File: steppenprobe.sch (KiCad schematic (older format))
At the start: 84 parts, among them J1 USB_C_Receptacle_USB2.0, J2 Conn_ST_STDC14, J4 Conn_01x16, Q1 2N7002, SW1 SW_SPDT, SW2 SW_Push, U1 FT2232H, U10 74LVC1G125, U11 74LVC1G125, U12 74LVC1G125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

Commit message: Replace FT2232H by FT2232HL
Old symbol is no longer in the library. It was a common symbol for
both LQFP and QFN and it is now individual symbols for different
packages.
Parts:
- U1: value FT2232H -> FT2232HL; symbol Interface_USB:FT2232H -> Interface_USB:FT2232HL
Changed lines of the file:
@@
 GPIO_A
 $Comp
-L Interface_USB:FT2232H U1
+L Interface_USB:FT2232HL U1
 U 1 1 5C60DA40
 P 7200 5950
 F 0 "U1" H 6200 8050 50  0000 C CNN
-F 1 "FT2232H" H 8100 8050 50  0000 C CNN
+F 1 "FT2232HL" H 8100 8050 50  0000 C CNN
 F 2 "Package_QFP:LQFP-64_10x10mm_P0.5mm" H 7200 5950 50  0001 C CNN
-F 3 "http://www.ftdichip.com/Products/ICs/FT2232H.html" H 7200 5950 50  0001 C CNN
+F 3 "https://www.ftdichip.com/Support/Documents/DataSheets/ICs/DS_FT2232H.pdf" H 7200 5950 50  0001 C CNN
 F 4 "FTDI" H 7200 5950 50  0001 C CNN "Manufacturer"
 F 5 "FT2232HL" H 7200 5950 50  0001 C CNN "MPN"

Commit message: Move 74xxGxx to a project library
The symbols in the upstream libraries use hidden power pins which
doesn't work in this design which needs different power rails on
different instances.

So far, a private modifed branch of the libraries was used. But,
becasue the upstream library won't be fix until KiCad 6 for
compatibility reasons, a project library has been created which
makes it easier to share this project.
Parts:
- U10, U11, U12, U5, U7, U8, U9: symbol 74xGxx:74LVC1G125 -> 74xxGxx_power_pins:74LVC1G125-74xGxx
- U6: symbol 74xGxx:74LVC1G126 -> 74xxGxx_power_pins:74LVC1G126-74xGxx
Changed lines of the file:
@@
 	11700 2800 11700 2750
 $Comp
-L 74xGxx:74LVC1G125 U8
+L 74xxGxx_power_pins:74LVC1G125-74xGxx U8
 U 1 1 5CA2CD85
 P 11800 2550
@@
 $EndComp
 $Comp
-L 74xGxx:74LVC1G125 U7
+L 74xxGxx_power_pins:74LVC1G125-74xGxx U7
 U 1 1 5C73B9C7
 P 11800 1650
@@
 	11750 3250 11750 3200
 $Comp
-L 74xGxx:74LVC1G125 U5
+L 74xxGxx_power_pins:74LVC1G125-74xGxx U5
 U 1 1 5C93EC63
 P 11750 3450
@@
 $EndComp
 $Comp
-L 74xGxx:74LVC1G125 U9
+L 74xxGxx_power_pins:74LVC1G125-74xGxx U9
 U 1 1 5C955E12
 P 11800 5200
@@
 $EndComp
 $Comp
-L 74xGxx:74LVC1G125 U10
+L 74xxGxx_power_pins:74LVC1G125-74xGxx U10
 U 1 1 5C980186
 P 11850 6350
@@
 	10850 3200 10850 4150
 $Comp
-L 74xGxx:74LVC1G126 U6
+L 74xxGxx_power_pins:74LVC1G126-74xGxx U6
 U 1 1 5CB0C088
 P 11750 4400
@@
 $EndComp
 $Comp
-L 74xGxx:74LVC1G125 U11
+L 74xxGxx_power_pins:74LVC1G125-74xGxx U11
 U 1 1 5C926BFE
 P 11850 8550
@@
 $EndComp
 $Comp
-L 74xGxx:74LVC1G125 U12
+L 74xxGxx_power_pins:74LVC1G125-74xGxx U12
 U 1 1 5C8DEFEB
 P 11900 7400

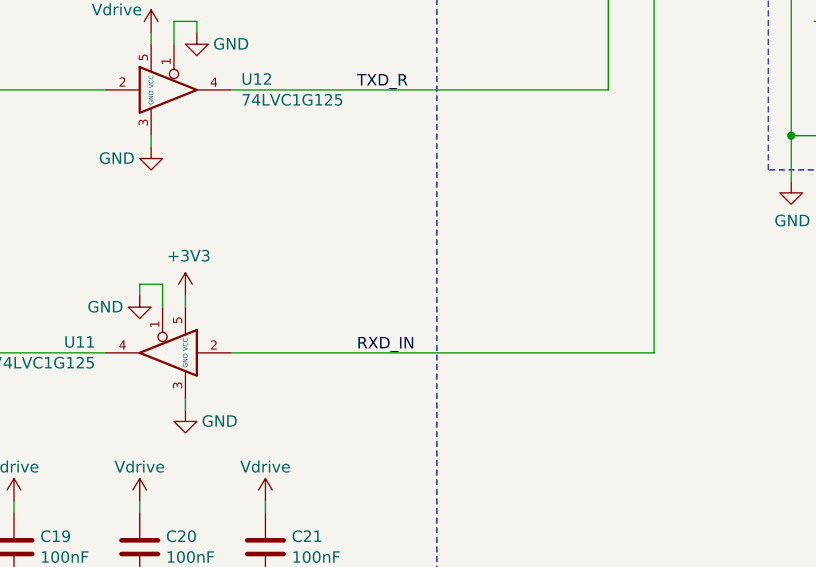
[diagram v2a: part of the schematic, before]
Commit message: Add pull up resistor to RXD_IN
To avoid spurious RX when floating.

Also some small tidy up of silkscreen designators.
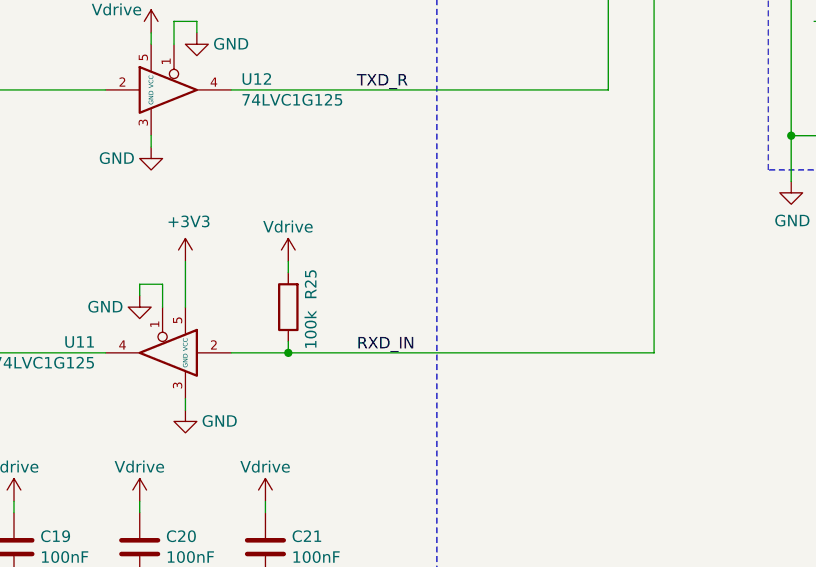
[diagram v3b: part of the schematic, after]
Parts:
- added R25: 100k, Resistor_SMD:R_0603_1608Metric, symbol Device:R
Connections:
- wire segments 370 -> 373
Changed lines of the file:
@@
 	12150 7400 13800 7400
-$Comp
-L power:+3V3 #PWR049
-U 1 1 5C93BEDD
-P 11950 8300
-F 0 "#PWR049" H 11950 8150 50  0001 C CNN
-F 1 "+3V3" H 11965 8473 50  0000 C CNN
-F 2 "" H 11950 8300 50  0001 C CNN
-F 3 "" H 11950 8300 50  0001 C CNN
-	1    11950 8300
-	1    0    0    -1
-$EndComp
 $Comp
 L 74xxGxx_power_pins:74LVC1G125-74xGxx U11
@@
 $EndComp
 Wire Wire Line
-	11950 8350 11950 8300
-Wire Wire Line
-	12150 8550 14000 8550
-Wire Wire Line
 	11600 8550 10750 8550
 Wire Wire Line
@@
 Text Label 8450 5550 0    50   ~ 0
 GPIO_D
+$Comp
+L Device:R R25
+U 1 1 5E57A95D
+P 12400 8350
+F 0 "R25" V 12300 8250 50  0000 C CNN
+F 1 "100k" V 12300 8450 50  0000 C CNN
+F 2 "Resistor_SMD:R_0603_1608Metric" V 12330 8350 50  0001 C CNN
+F 3 "~" H 12400 8350 50  0001 C CNN
+F 4 "C25803" H 12400 8350 50  0001 C CNN "LCSC_PN"
+	1    12400 8350
+	-1   0    0    1
+$EndComp
+Wire Wire Line
+	11950 8350 11950 8150
+$Comp
+L power:+3V3 #PWR049
+U 1 1 5C93BEDD
+P 11950 8150
+F 0 "#PWR049" H 11950 8000 50  0001 C CNN
+F 1 "+3V3" H 11965 8323 50  0000 C CNN
+F 2 "" H 11950 8150 50  0001 C CNN
+F 3 "" H 11950 8150 50  0001 C CNN
+	1    11950 8150
+	1    0    0    -1
+$EndComp
+Wire Wire Line
+	12400 8550 14000 8550
+Connection ~ 12400 8550
+Wire Wire Line
+	12150 8550 12400 8550
+Wire Wire Line
+	12400 8550 12400 8500
+Wire Wire Line
+	12400 8150 12400 8200
+$Comp
+L power:Vdrive #PWR067
+U 1 1 5E57CDC9
+P 12400 8150
+F 0 "#PWR067" H 12200 8000 50  0001 C CNN
+F 1 "Vdrive" H 12400 8300 50  0000 C CNN
+F 2 "" H 12400 8150 50  0001 C CNN
+F 3 "" H 12400 8150 50  0001 C CNN
+	1    12400 8150
+	1    0    0    -1
+$EndComp
 $EndSCHEMATC

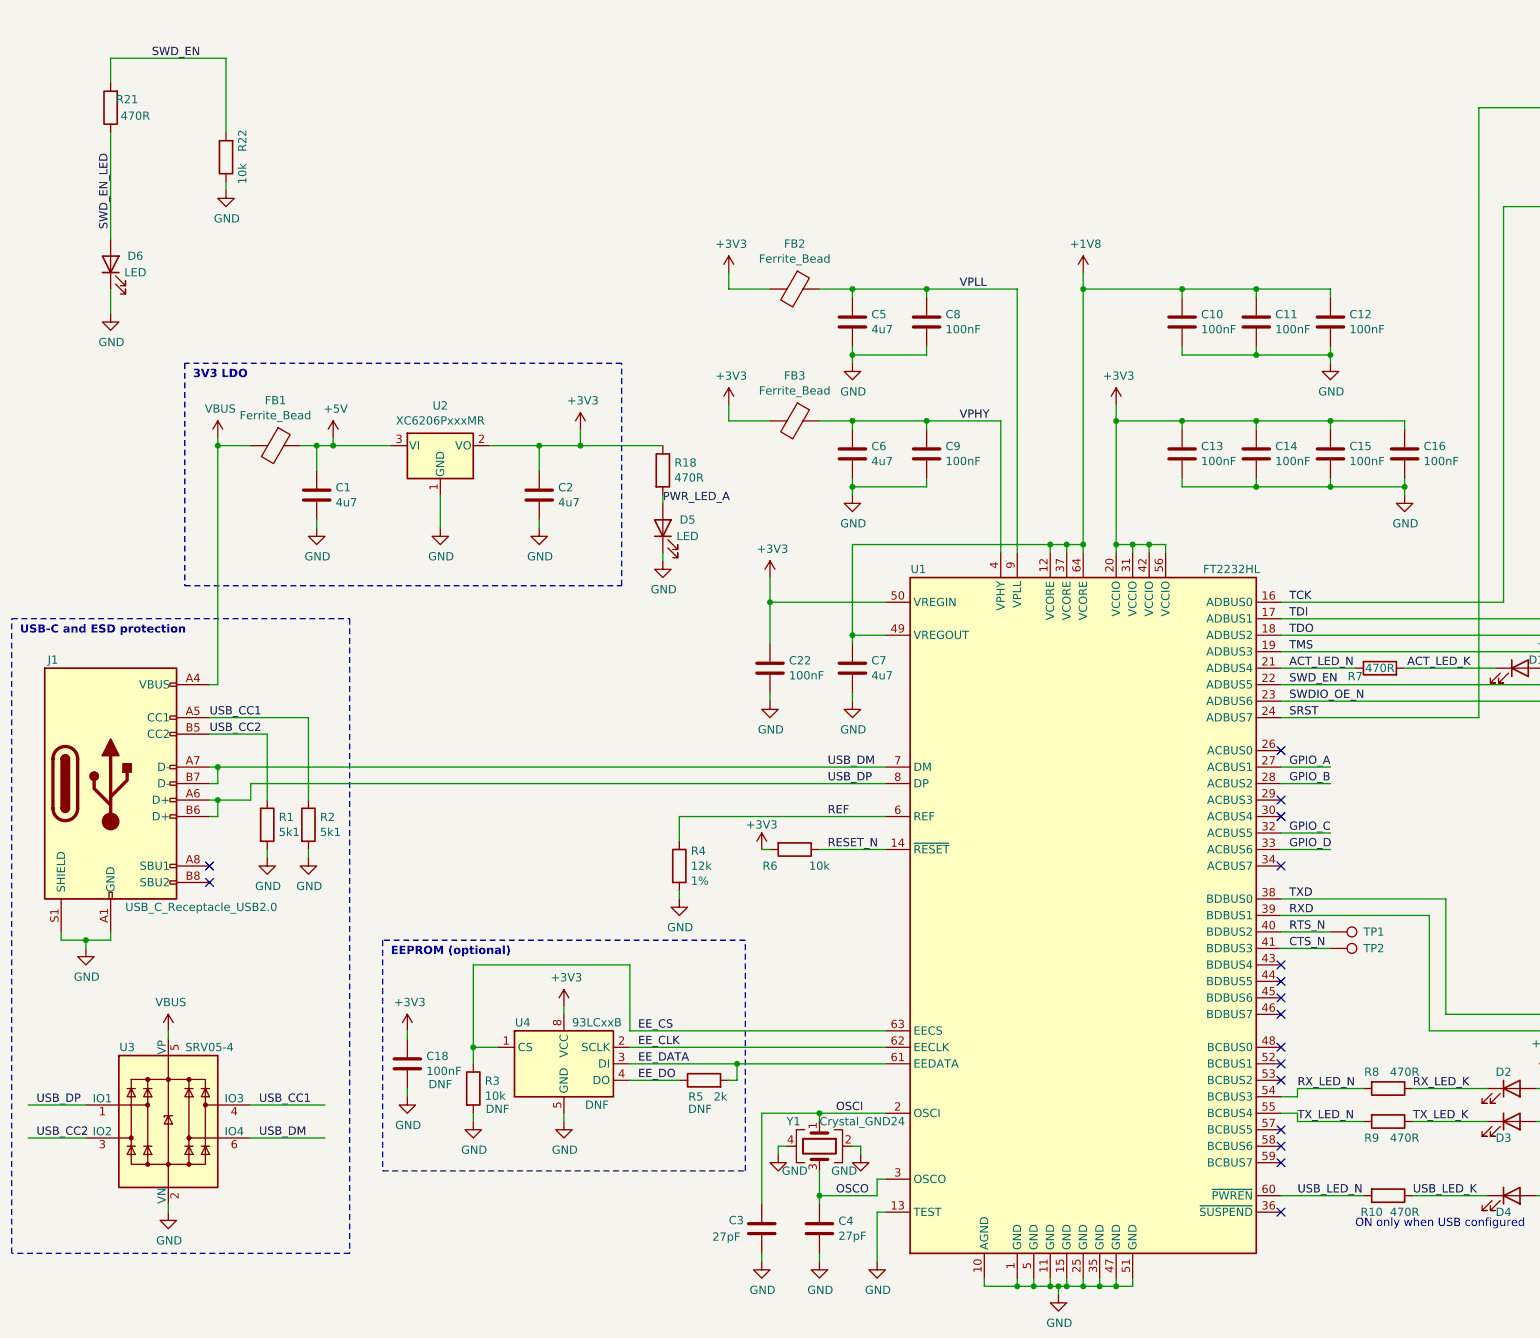
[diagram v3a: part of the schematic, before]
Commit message: LED resistors: 470R -> 1k     They were too bright. 1k may still be a bit too bright but if the current is reduced further, the LEDs which blink for brief instants, like the JTAG/SWD activity, get harder to see. Different resistors could be used for different LEDs, but for BOM simplicity, it was decided to stick with 1k everywhere.
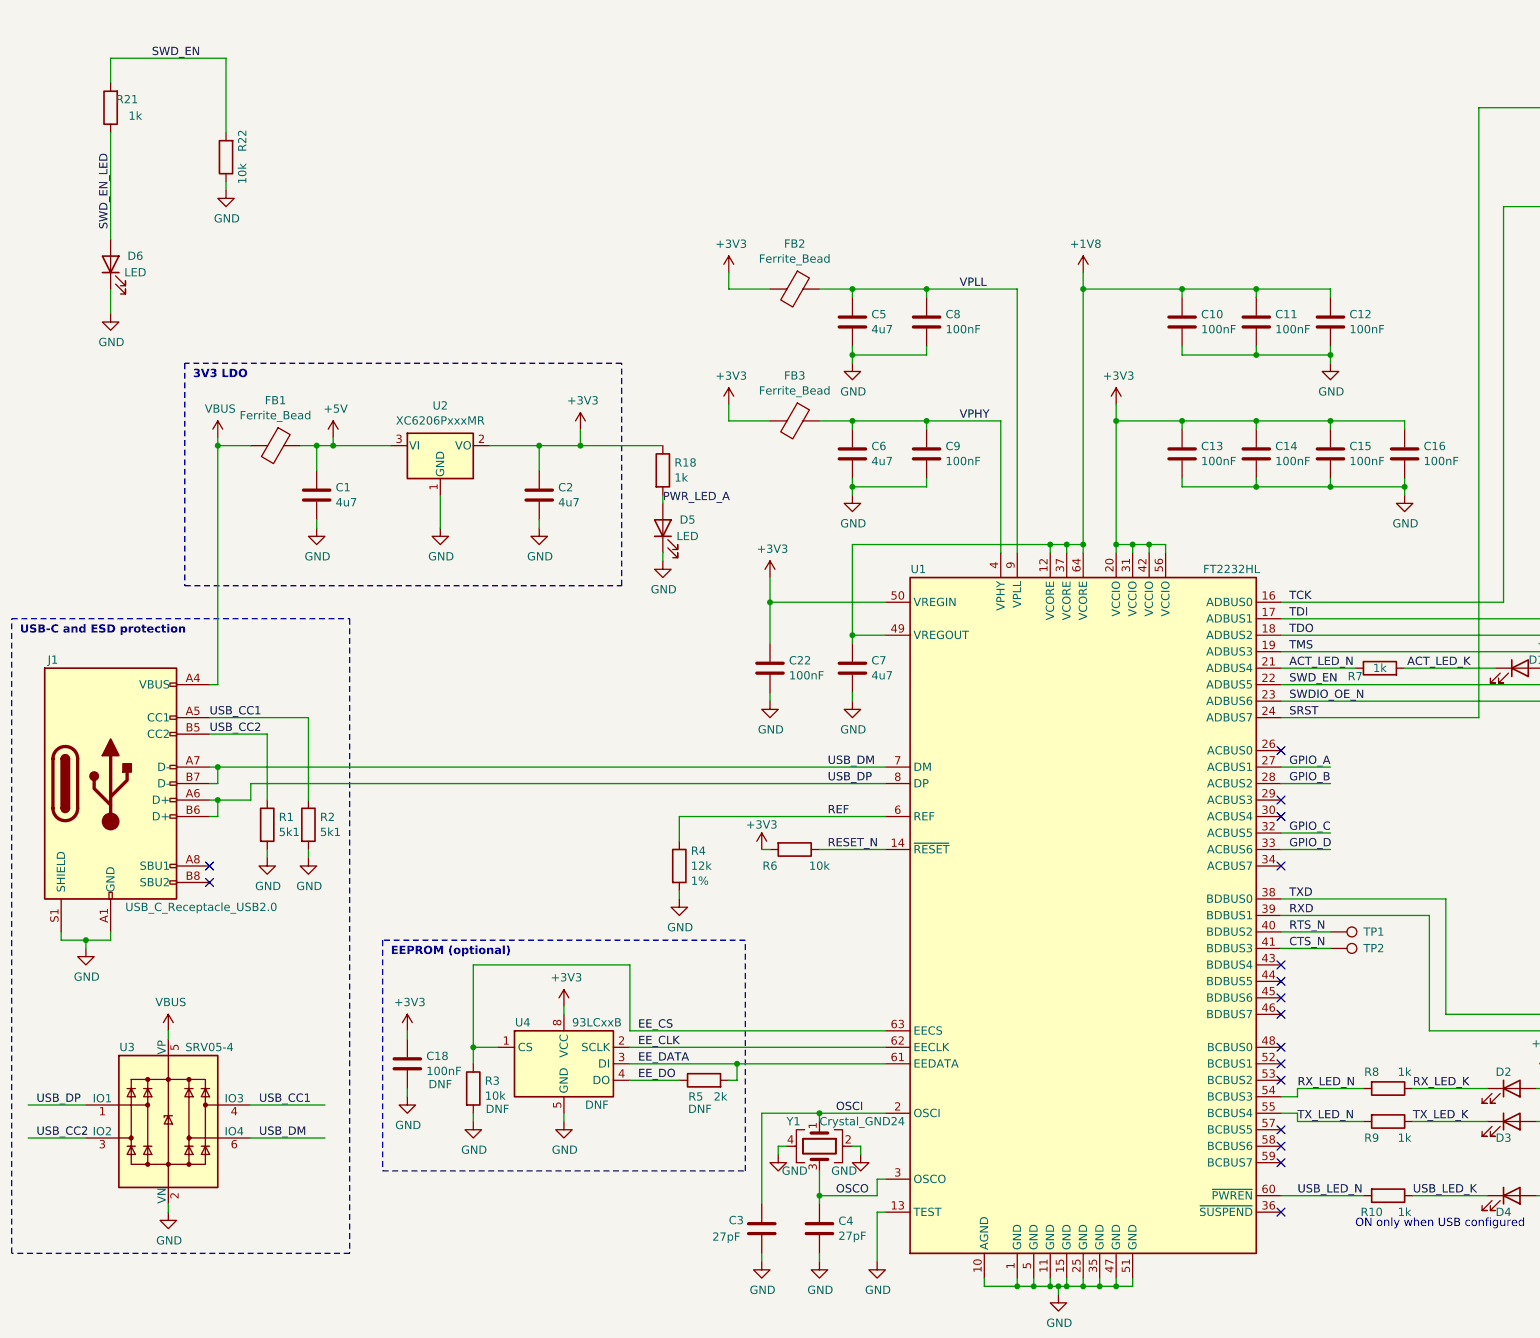
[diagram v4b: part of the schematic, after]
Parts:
- R10, R18, R21, R7, R8, R9: value 470R -> 1k; LCSC_PN C23179 -> C21190
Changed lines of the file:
@@
 P 9050 7000
 F 0 "R8" V 8950 6900 50  0000 C CNN
-F 1 "470R" V 8950 7100 50  0000 C CNN
+F 1 "1k" V 8950 7100 50  0000 C CNN
 F 2 "Resistor_SMD:R_0603_1608Metric" V 8980 7000 50  0001 C CNN
 F 3 "~" H 9050 7000 50  0001 C CNN
-F 4 "C23179" H 9050 7000 50  0001 C CNN "LCSC_PN"
+F 4 "C21190" H 9050 7000 50  0001 C CNN "LCSC_PN"
 	1    9050 7000
 	0    1    1    0
@@
 P 9050 7200
 F 0 "R9" V 9150 7100 50  0000 C CNN
-F 1 "470R" V 9150 7300 50  0000 C CNN
+F 1 "1k" V 9150 7300 50  0000 C CNN
 F 2 "Resistor_SMD:R_0603_1608Metric" V 8980 7200 50  0001 C CNN
 F 3 "~" H 9050 7200 50  0001 C CNN
-F 4 "C23179" H 9050 7200 50  0001 C CNN "LCSC_PN"
+F 4 "C21190" H 9050 7200 50  0001 C CNN "LCSC_PN"
 	1    9050 7200
 	0    1    1    0
@@
 P 9050 7650
 F 0 "R10" V 9150 7550 50  0000 C CNN
-F 1 "470R" V 9150 7750 50  0000 C CNN
+F 1 "1k" V 9150 7750 50  0000 C CNN
 F 2 "Resistor_SMD:R_0603_1608Metric" V 8980 7650 50  0001 C CNN
 F 3 "~" H 9050 7650 50  0001 C CNN
-F 4 "C23179" H 9050 7650 50  0001 C CNN "LCSC_PN"
+F 4 "C21190" H 9050 7650 50  0001 C CNN "LCSC_PN"
 	1    9050 7650
 	0    1    1    0
@@
 P 4650 3250
 F 0 "R18" H 4720 3296 50  0000 L CNN
-F 1 "470R" H 4720 3205 50  0000 L CNN
+F 1 "1k" H 4720 3205 50  0000 L CNN
 F 2 "Resistor_SMD:R_0603_1608Metric" V 4580 3250 50  0001 C CNN
 F 3 "~" H 4650 3250 50  0001 C CNN
-F 4 "C23179" H 4650 3250 50  0001 C CNN "LCSC_PN"
+F 4 "C21190" H 4650 3250 50  0001 C CNN "LCSC_PN"
 	1    4650 3250
 	1    0    0    -1
@@
 P 1300 1050
 F 0 "R21" H 1200 1000 50  0000 C CNN
-F 1 "470R" H 1150 1100 50  0000 C CNN
+F 1 "1k" H 1150 1100 50  0000 C CNN
 F 2 "Resistor_SMD:R_0603_1608Metric" V 1230 1050 50  0001 C CNN
 F 3 "~" H 1300 1050 50  0001 C CNN
-F 4 "C23179" H 1300 1050 50  0001 C CNN "LCSC_PN"
+F 4 "C21190" H 1300 1050 50  0001 C CNN "LCSC_PN"
 	1    1300 1050
 	-1   0    0    1
@@
 P 9000 4450
 F 0 "R7" V 8950 4600 50  0000 C CNN
-F 1 "470R" V 9000 4450 50  0000 C CNN
+F 1 "1k" V 9000 4450 50  0000 C CNN
 F 2 "Resistor_SMD:R_0603_1608Metric" V 8930 4450 50  0001 C CNN
 F 3 "~" H 9000 4450 50  0001 C CNN
-F 4 "C23179" H 9000 4450 50  0001 C CNN "LCSC_PN"
+F 4 "C21190" H 9000 4450 50  0001 C CNN "LCSC_PN"
 	1    9000 4450
 	0    -1   -1   0

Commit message: Tolerance and Type information added for BOM
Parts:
- C1, C10, C11, C12, C13, C14, C15, C16, C17, C19, C2, C20, C21, C22, C5, C6, C7, C8, C9: Tolerance (none) -> 10%; Type (none) -> X5R/X7R
- C3, C4: Tolerance (none) -> 5%; Type (none) -> C0G
- R1, R10, R11, R12, R13, R14, R15, R16, R17, R18, R19, R2, R20, R21, R22, R23, R24, R25, R6, R7, R8, R9: Tolerance (none) -> 5%

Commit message: Add 10-way Samtec connector as alternative to the 14-way.
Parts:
- J2: MPN FTSH-107-01-F-DV-K -> FTSH-107-01-F-DV-K (if 14-way); MPN2 (none) -> FTSH-105-01-F-DV-K (if 10 way); Manufacturer2 (none) -> Samtec
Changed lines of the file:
@@
 F 2 "Connector_PinHeader_1.27mm:PinHeader_2x07_P1.27mm_Vertical_SMD" H 15550 3100 50  0001 C CNN
 F 3 "https://www.st.com/content/ccc/resource/technical/document/user_manual/group1/99/49/91/b6/b2/3a/46/e5/DM00526767/files/DM00526767.pdf/jcr:content/translations/en.DM00526767.pdf" V 15200 1850 50  0001 C CNN
-F 4 "FTSH-107-01-F-DV-K" H 15550 3100 50  0001 C CNN "MPN"
+F 4 "FTSH-107-01-F-DV-K (if 14-way)" H 15550 3100 50  0001 C CNN "MPN"
 F 5 "Samtec" H 15550 3100 50  0001 C CNN "Manufacturer"
+F 6 "FTSH-105-01-F-DV-K (if 10 way)" H 15550 3100 50  0001 C CNN "MPN2"
+F 7 "Samtec" H 15550 3100 50  0001 C CNN "Manufacturer2"
 	1    15550 3100
 	-1   0    0    -1
